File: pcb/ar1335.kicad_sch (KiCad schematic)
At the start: 46 parts

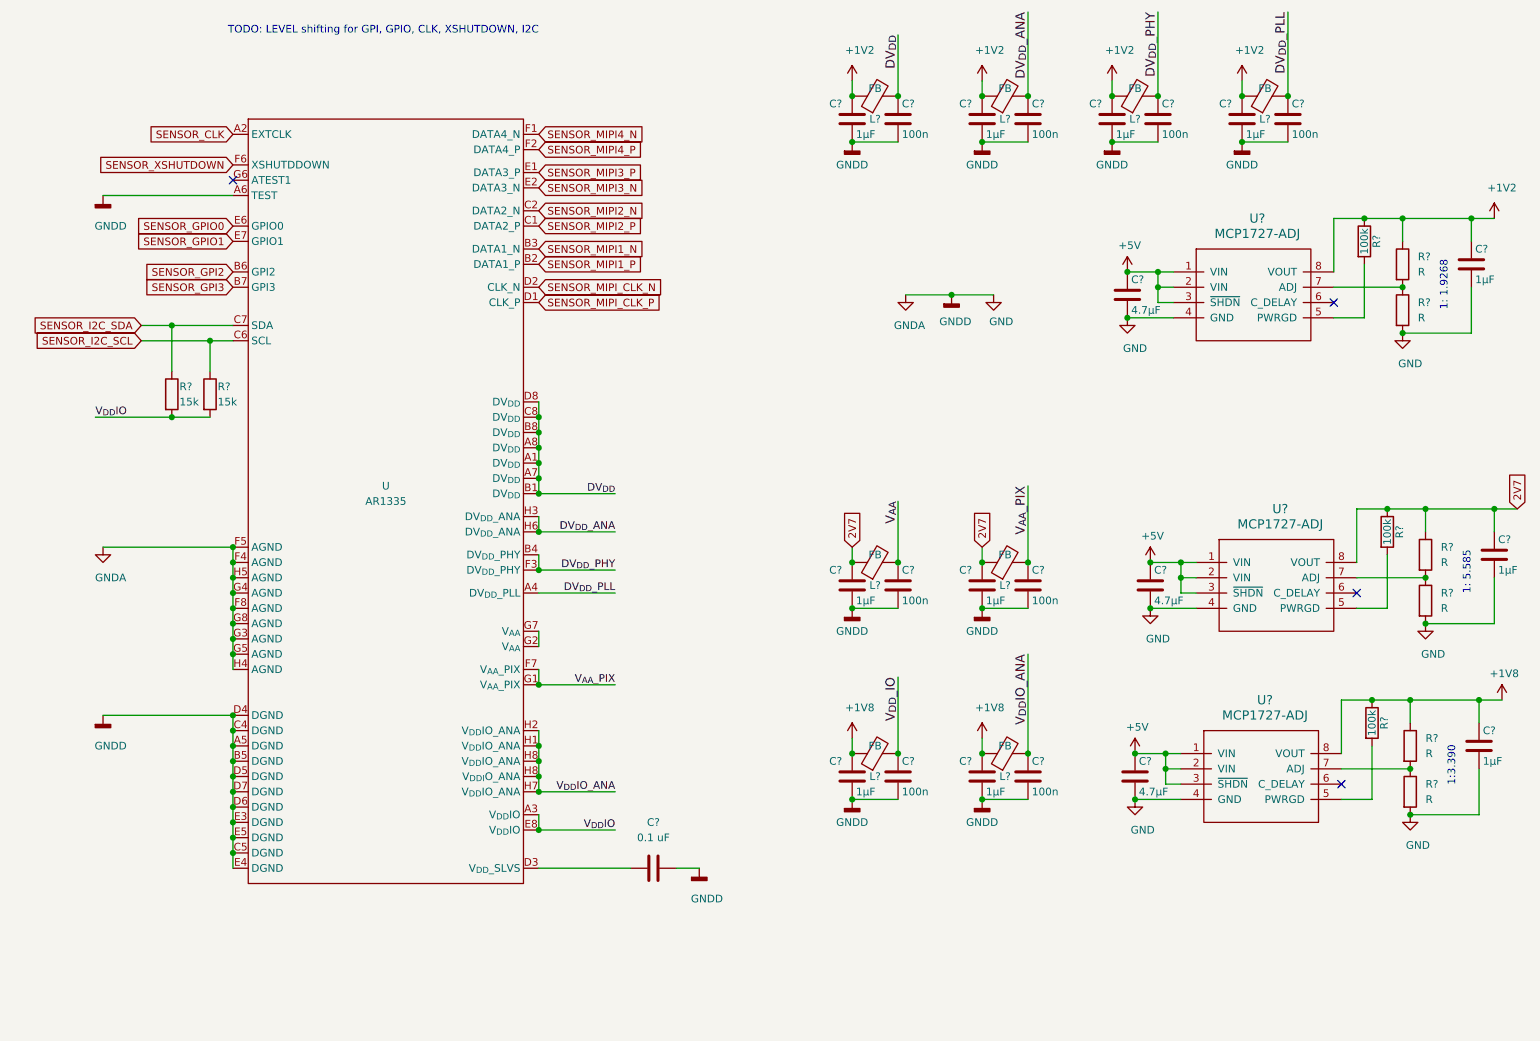
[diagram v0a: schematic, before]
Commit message: refinements; add ar1335 footprint
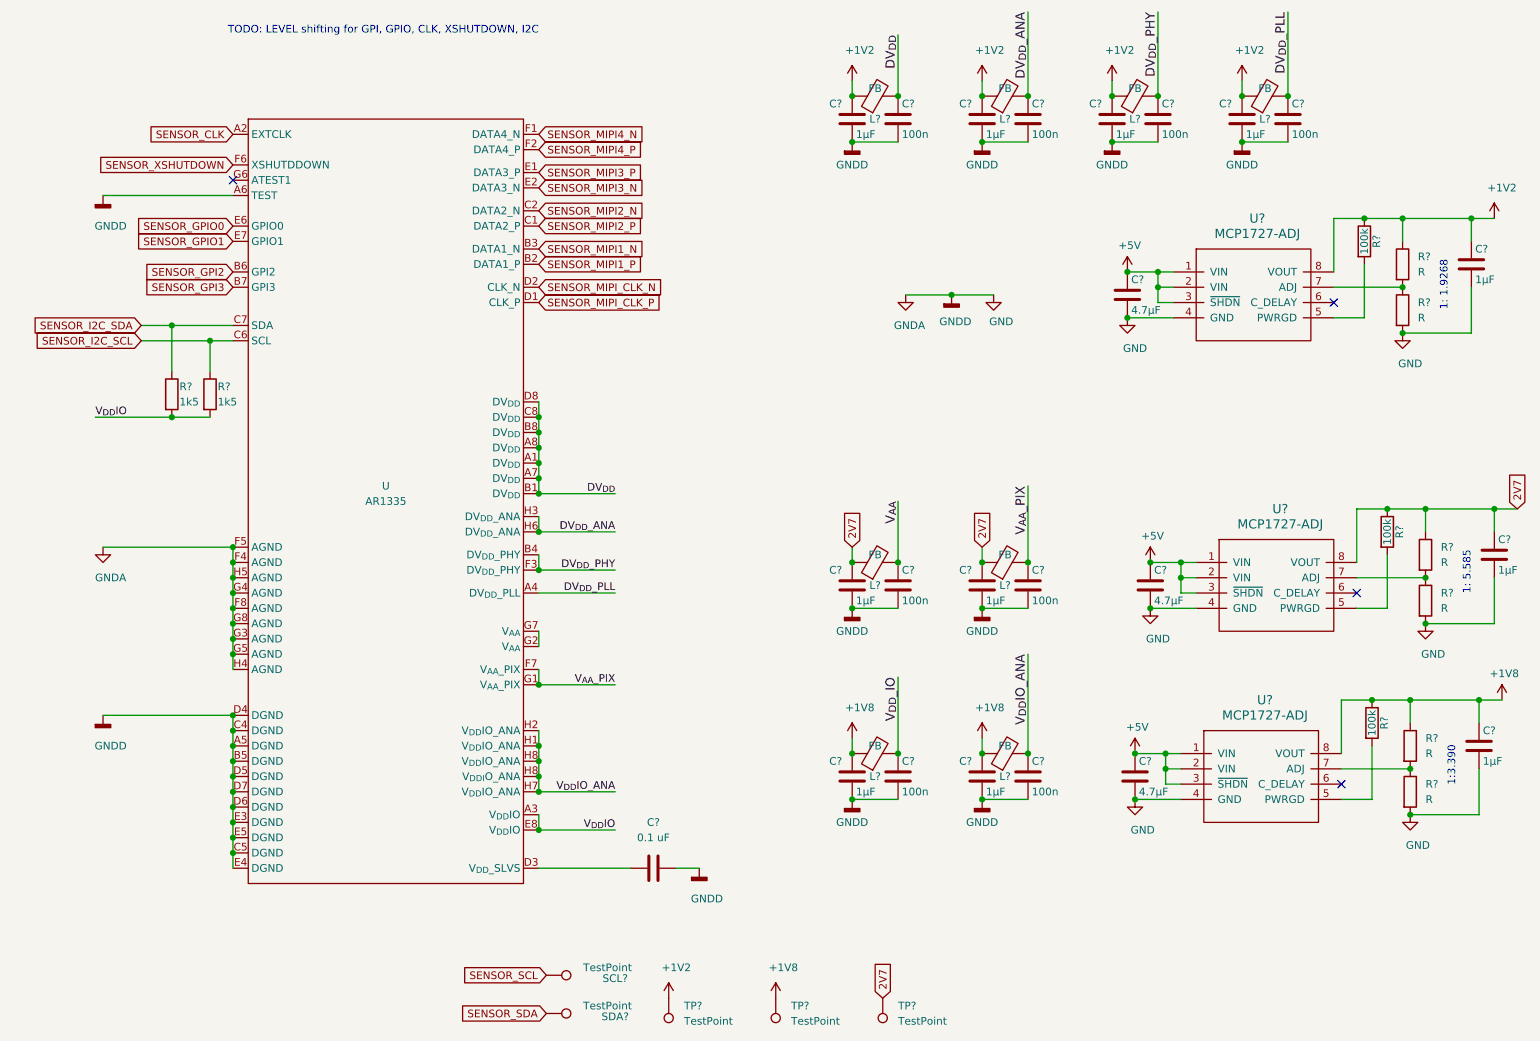
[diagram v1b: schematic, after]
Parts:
- added SCL?, SDA?: TestPoint, Connectors_TestPoints:Test_Point_Pad_2.0x2.0mm, symbol Connector:TestPoint
- added TP? (x3): TestPoint, symbol Connector:TestPoint
- R? (x2): value 15k -> 1k5
- U: footprint (none) -> ar1335:ODCSP63
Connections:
- net +1V2: now also TP?.1
- net +1V8: now also TP?.1
- net 2V7: now also TP?.1
- new net SENSOR_SCL: SCL?.1
- new net SENSOR_SDA: SDA?.1
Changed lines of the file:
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@@
     (effects (font (size 1.27 1.27)) (justify left))
+  )
+  (global_label "SENSOR_SCL" (shape input) (at 100.33 182.88 180)    (property "Intersheet References" "${INTERSHEET_REFS}" (id 0) (at 84.4186 182.8006 0)
+      (effects (font (size 1.27 1.27)) (justify right) hide)
+    )
+    (effects (font (size 1.27 1.27)) (justify right))
+  )
+  (global_label "SENSOR_SDA" (shape input) (at 100.33 189.23 180)    (property "Intersheet References" "${INTERSHEET_REFS}" (id 0) (at 84.3581 189.1506 0)
+      (effects (font (size 1.27 1.27)) (justify right) hide)
+    )
+    (effects (font (size 1.27 1.27)) (justify right))
   )
   (global_label "2V7" (shape input) (at 151.13 111.76 90)    (property "Intersheet References" "${INTERSHEET_REFS}" (id 0) (at 151.0506 104.3153 90)
@@
     (effects (font (size 1.27 1.27)) (justify left))
   )
+  (global_label "2V7" (shape input) (at 156.21 186.69 90)    (property "Intersheet References" "${INTERSHEET_REFS}" (id 0) (at 156.1306 179.2453 90)
+      (effects (font (size 1.27 1.27)) (justify left) hide)
+    )
+    (effects (font (size 1.27 1.27)) (justify left))
+  )
   (global_label "2V7" (shape input) (at 172.72 111.76 90)    (property "Intersheet References" "${INTERSHEET_REFS}" (id 0) (at 172.6406 104.3153 90)
       (effects (font (size 1.27 1.27)) (justify left) hide)
@@
     (effects (font (size 1.27 1.27)) (justify left))
   )
+  (symbol (lib_id "Connector:TestPoint") (at 100.33 182.88 270) (unit 1)
+    (in_bom yes) (on_board yes)
+    (property "Reference" "SCL?" (id 0) (at 111.76 184.15 90)
+      (effects (font (size 1.27 1.27)) (justify bottom))
+    )
+    (property "Value" "TestPoint" (id 1) (at 110.49 181.61 90))
+    (property "Footprint" "Connectors_TestPoints:Test_Point_Pad_2.0x2.0mm" (id 2) (at 100.33 182.88 0)
+      (effects (font (size 1.27 1.27)) hide)
+    )
+    (property "Datasheet" "" (id 3) (at 100.33 182.88 0)
+      (effects (font (size 1.27 1.27)) hide)
+    )
+  )
+  (symbol (lib_id "Connector:TestPoint") (at 100.33 189.23 270) (unit 1)
+    (in_bom yes) (on_board yes)
+    (property "Reference" "SDA?" (id 0) (at 111.76 190.5 90)
+      (effects (font (size 1.27 1.27)) (justify bottom))
+    )
+    (property "Value" "TestPoint" (id 1) (at 110.49 187.96 90))
+    (property "Footprint" "Connectors_TestPoints:Test_Point_Pad_2.0x2.0mm" (id 2) (at 100.33 189.23 0)
+      (effects (font (size 1.27 1.27)) hide)
+    )
+    (property "Datasheet" "" (id 3) (at 100.33 189.23 0)
+      (effects (font (size 1.27 1.27)) hide)
+    )
+  )
+  (symbol (lib_id "Connector:TestPoint") (at 120.65 186.69 180) (unit 1)
+    (in_bom yes) (on_board yes)
+    (property "Reference" "TP?" (id 0) (at 123.19 187.96 0)
+      (effects (font (size 1.27 1.27)) (justify right))
+    )
+    (property "Value" "TestPoint" (id 1) (at 123.19 190.5 0)
+      (effects (font (size 1.27 1.27)) (justify right))
+    )
+    (property "Footprint" "" (id 2) (at 115.57 186.69 0)
+      (effects (font (size 1.27 1.27)) hide)
+    )
+    (property "Datasheet" "~" (id 3) (at 115.57 186.69 0)
+      (effects (font (size 1.27 1.27)) hide)
+    )
+  )
+  (symbol (lib_id "Connector:TestPoint") (at 138.43 186.69 180) (unit 1)
+    (in_bom yes) (on_board yes)
+    (property "Reference" "TP?" (id 0) (at 140.97 187.96 0)
+      (effects (font (size 1.27 1.27)) (justify right))
+    )
+    (property "Value" "TestPoint" (id 1) (at 140.97 190.5 0)
+      (effects (font (size 1.27 1.27)) (justify right))
+    )
+    (property "Footprint" "" (id 2) (at 133.35 186.69 0)
+      (effects (font (size 1.27 1.27)) hide)
+    )
+    (property "Datasheet" "~" (id 3) (at 133.35 186.69 0)
+      (effects (font (size 1.27 1.27)) hide)
+    )
+  )
+  (symbol (lib_id "Connector:TestPoint") (at 156.21 186.69 180) (unit 1)
+    (in_bom yes) (on_board yes)
+    (property "Reference" "TP?" (id 0) (at 158.75 187.96 0)
+      (effects (font (size 1.27 1.27)) (justify right))
+    )
+    (property "Value" "TestPoint" (id 1) (at 158.75 190.5 0)
+      (effects (font (size 1.27 1.27)) (justify right))
+    )
+    (property "Footprint" "" (id 2) (at 151.13 186.69 0)
+      (effects (font (size 1.27 1.27)) hide)
+    )
+    (property "Datasheet" "~" (id 3) (at 151.13 186.69 0)
+      (effects (font (size 1.27 1.27)) hide)
+    )
+  )
+  (symbol (lib_id "power:+1V2") (at 120.65 186.69 0) (unit 1)
+    (in_bom yes) (on_board yes)
+    (property "Reference" "#PWR?" (id 0) (at 120.65 190.5 0)
+      (effects (font (size 1.27 1.27)) hide)
+    )
+    (property "Value" "+1V2" (id 1) (at 121.92 181.61 0))
+    (property "Footprint" "" (id 2) (at 120.65 186.69 0)
+      (effects (font (size 1.27 1.27)) hide)
+    )
+    (property "Datasheet" "" (id 3) (at 120.65 186.69 0)
+      (effects (font (size 1.27 1.27)) hide)
+    )
+  )
+  (symbol (lib_id "power:+1V8") (at 138.43 186.69 0) (unit 1)
+    (in_bom yes) (on_board yes)
+    (property "Reference" "#PWR?" (id 0) (at 138.43 190.5 0)
+      (effects (font (size 1.27 1.27)) hide)
+    )
+    (property "Value" "+1V8" (id 1) (at 139.7 181.61 0))
+    (property "Footprint" "" (id 2) (at 138.43 186.69 0)
+      (effects (font (size 1.27 1.27)) hide)
+    )
+    (property "Datasheet" "" (id 3) (at 138.43 186.69 0)
+      (effects (font (size 1.27 1.27)) hide)
+    )
+  )
   (symbol (lib_id "power:+1V2") (at 151.13 34.29 0) (unit 1)
     (in_bom yes) (on_board yes)
@@
       (effects (font (size 1.27 1.27)) (justify left))
     )
-    (property "Value" "15k" (id 1) (at 39.37 87.63 0)
+    (property "Value" "1k5" (id 1) (at 39.37 87.63 0)
       (effects (font (size 1.27 1.27)) (justify left))
     )
@@
       (effects (font (size 1.27 1.27)) (justify left))
     )
-    (property "Value" "15k" (id 1) (at 45.72 87.63 0)
+    (property "Value" "1k5" (id 1) (at 45.72 87.63 0)
       (effects (font (size 1.27 1.27)) (justify left))
     )
@@
     (property "Reference" "U" (id 0) (at 73.66 101.6 0))
     (property "Value" "AR1335" (id 1) (at 73.66 104.14 0))
-    (property "Footprint" "" (id 2) (at 73.66 107.95 0)
-      (effects (font (size 1.27 1.27)) hide)
-    )
+    (property "Footprint" "ar1335:ODCSP63" (id 2) (at 73.66 107.95 0)
+      (effects (font (size 1.27 1.27)) hide)
+    )

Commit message: Change Plans: two image sensors
* Redo power management
* Add level shifters
* Intention to use both image sensors on the same board
* Add Pmod & LEDs
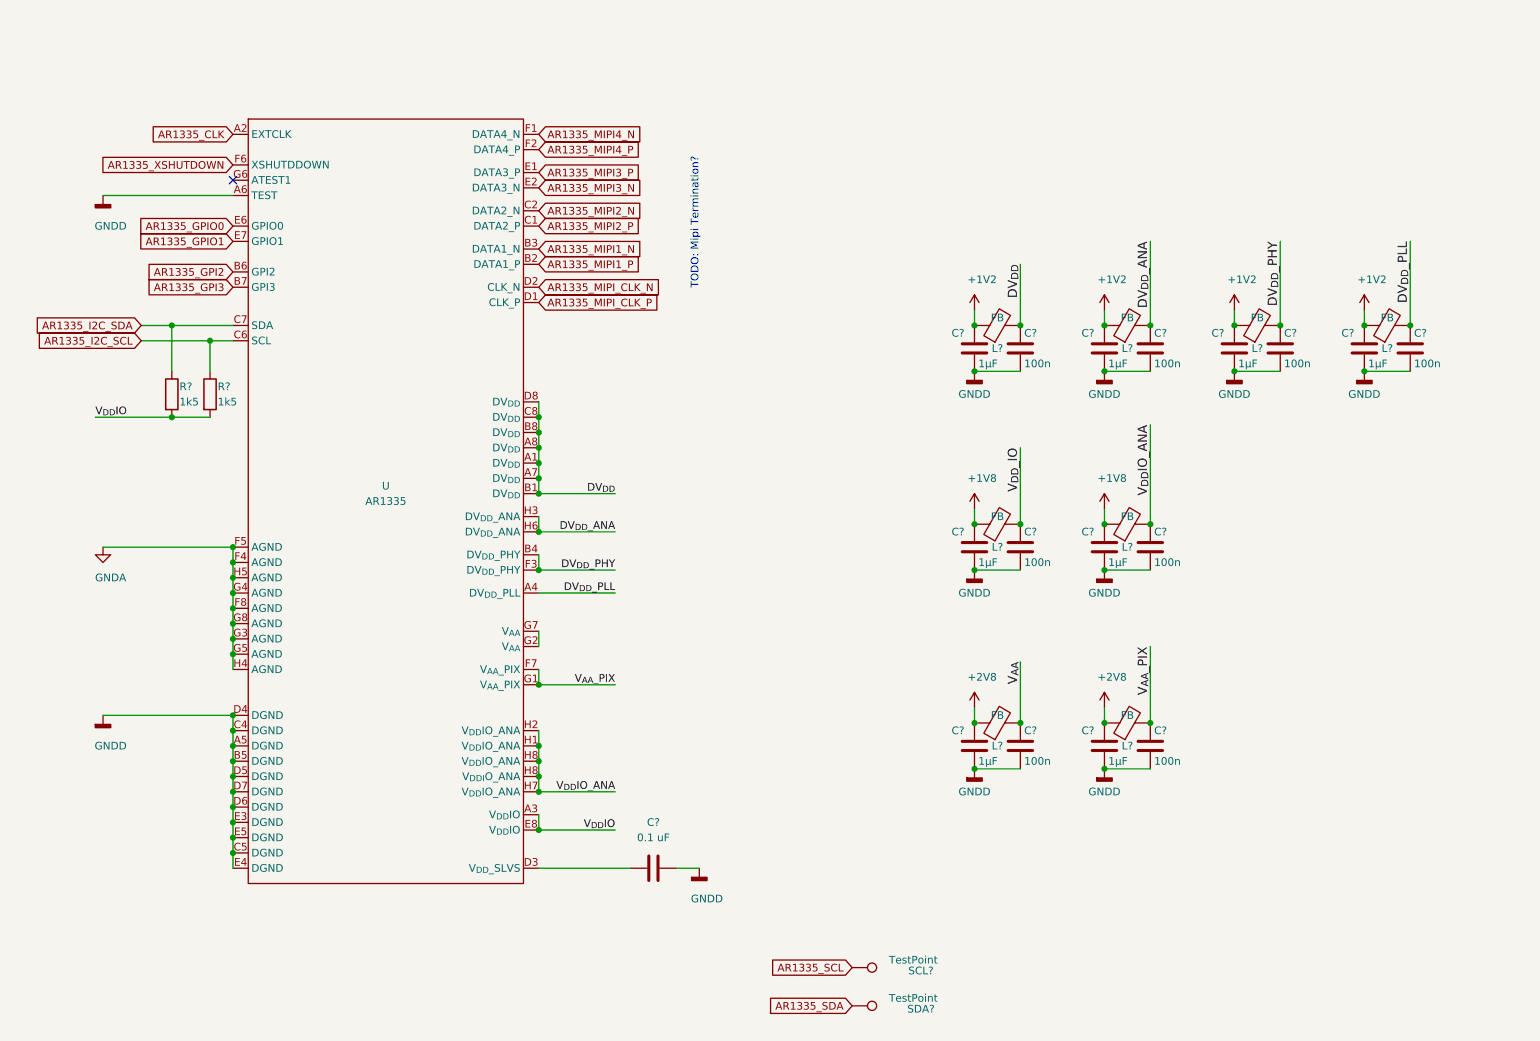
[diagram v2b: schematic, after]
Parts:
- removed C? (x3): 4.7µF, Capacitors_SMD:C_0603_HandSoldering, symbol Device:C
- removed C? (x3): 1µF, Capacitors_SMD:C_0402, symbol Device:C
- removed R? (x6): R, symbol Device:R
- removed R? (x3): 100k, Resistors_SMD:R_0603_HandSoldering, symbol Device:R
- removed TP? (x3): TestPoint, symbol Connector:TestPoint
- removed U? (x3): MCP1727-ADJ, symbol parts:MCP1727-ADJ
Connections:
- net 2V7 renamed +2V8
- net GND renamed GNDD
- net GNDD: no longer U.F4 (AGND), U.F5 (AGND), U.F8 (AGND), U.G3 (AGND), U.G4 (AGND), U.G5 (AGND), U.G8 (AGND), U.H4 (AGND), U.H5 (AGND)
- net SENSOR_CLK renamed AR1335_CLK
- net SENSOR_GPI2 renamed AR1335_GPI2
- net SENSOR_GPI3 renamed AR1335_GPI3
- net SENSOR_GPIO0 renamed AR1335_GPIO0
- net SENSOR_GPIO1 renamed AR1335_GPIO1
- net SENSOR_I2C_SCL renamed AR1335_I2C_SCL
- net SENSOR_I2C_SDA renamed AR1335_I2C_SDA
- net SENSOR_MIPI1_N renamed AR1335_MIPI1_N
- net SENSOR_MIPI1_P renamed AR1335_MIPI1_P
- net SENSOR_MIPI2_N renamed AR1335_MIPI2_N
- net SENSOR_MIPI2_P renamed AR1335_MIPI2_P
- net SENSOR_MIPI3_N renamed AR1335_MIPI3_N
- net SENSOR_MIPI3_P renamed AR1335_MIPI3_P
- net SENSOR_MIPI4_N renamed AR1335_MIPI4_N
- net SENSOR_MIPI4_P renamed AR1335_MIPI4_P
- net SENSOR_MIPI_CLK_N renamed AR1335_MIPI_CLK_N
- net SENSOR_MIPI_CLK_P renamed AR1335_MIPI_CLK_P
- net SENSOR_SCL renamed AR1335_SCL
- net SENSOR_SDA renamed AR1335_SDA
- net SENSOR_XSHUTDOWN renamed AR1335_XSHUTDOWN
- new net GNDA: U.F4 (AGND), U.F5 (AGND), U.F8 (AGND), U.G3 (AGND), U.G4 (AGND), U.G5 (AGND), U.G8 (AGND), U.H4 (AGND), U.H5 (AGND)
- no-connect marks 4 -> 1
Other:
- note added: "TODO: Mipi Termination?"
- note removed: "1: 1.9268"
- note removed: "1: 5.585"
- note removed: "1:3.390"
- note removed: "TODO: LEVEL shifting for GPI, GPIO, CLK, XSHUTDOWN, I2C"
- moved on the sheet: C?, L?, SCL?, SDA?

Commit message: add i2c addresses
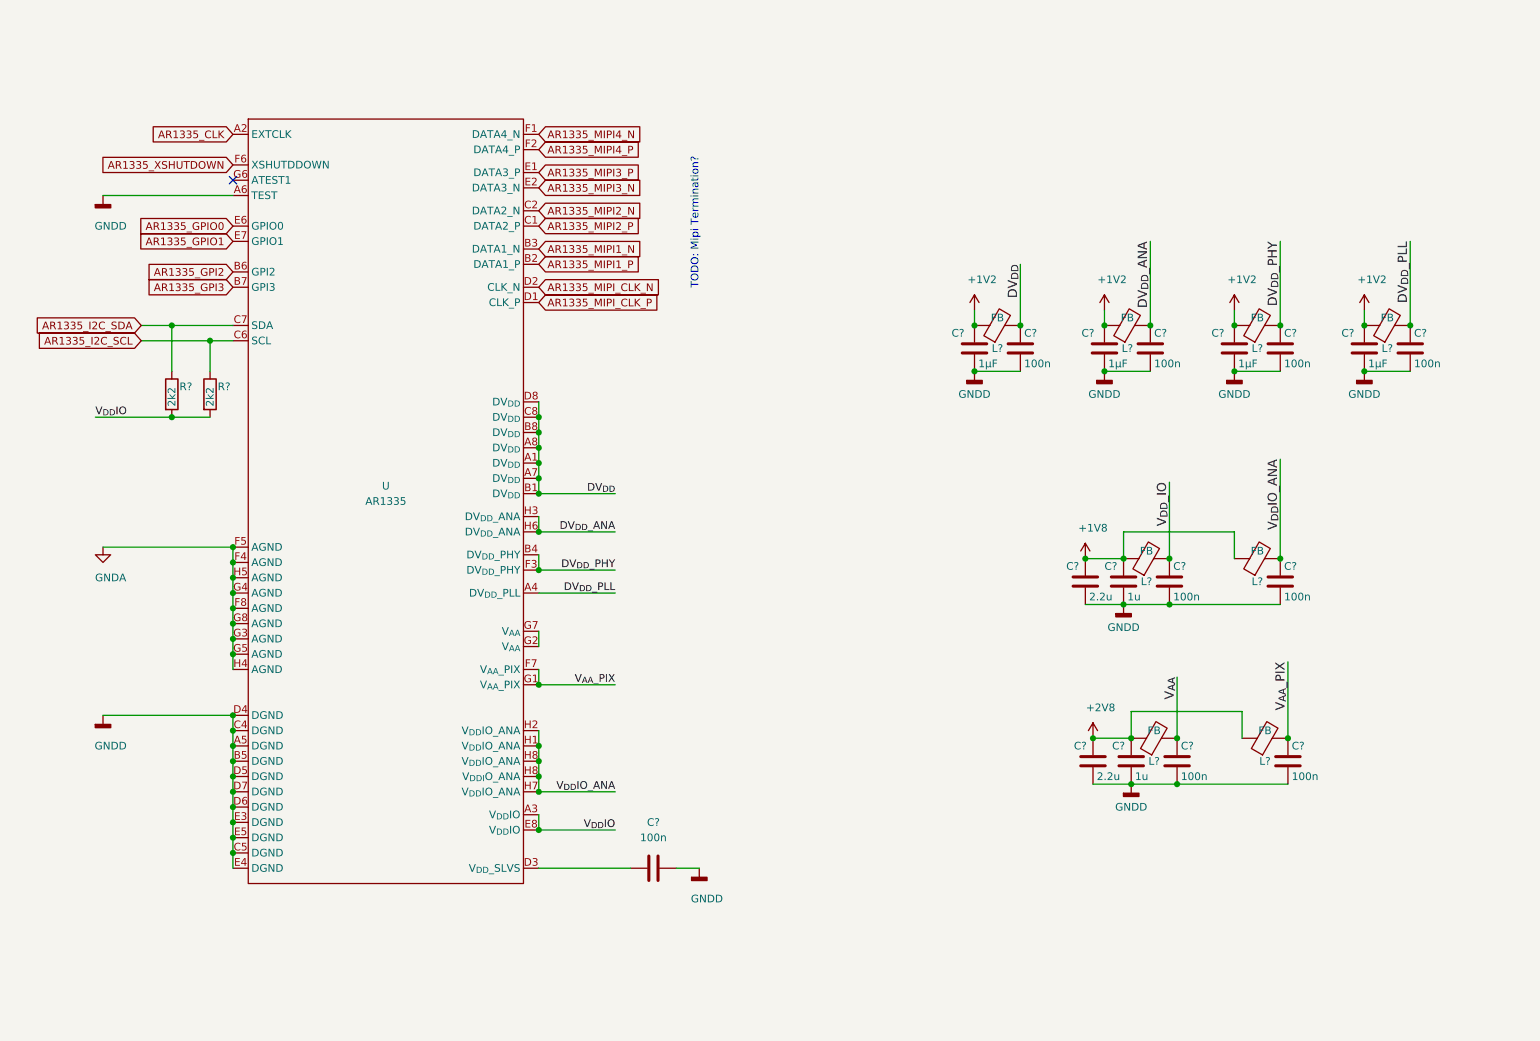
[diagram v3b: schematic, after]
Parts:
- removed C? (x3): 1µF, Capacitors_SMD:C_0402, symbol Device:C
- removed C? (x2): 100n, Capacitors_SMD:C_0402, symbol Device:C
- removed L? (x2): FB, parts:ferrite_bead_0402_handsoldering, symbol Device:FerriteBead
- removed SCL?, SDA?: TestPoint, Connectors_TestPoints:Test_Point_Pad_2.0x2.0mm, symbol Connector:TestPoint
- added C? (x2): 100n, Capacitors_SMD:C_0402, symbol Device:C
- added C? (x2): 2.2u, symbol Device:C
- added C?: 1u, Capacitors_SMD:C_0402, symbol Device:C
- added L? (x2): FB, parts:ferrite_bead_0402_handsoldering, symbol Device:FerriteBead
- C?: value 0.1 uF -> 100n
- C?: value 1µF -> 1u
- R? (x2): value 1k5 -> 2k2
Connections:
- net +1V8: now also C?.1, C?.1, L?.1, L?.1
- net +2V8: now also C?.1
- net GNDD: now also C?.2, C?.2, C?.2, C?.2, C?.2
- net V_{DD}IO_ANA: now also C?.1, L?.2
- net V_{DD}_IO: now also C?.1, L?.2
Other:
- moved on the sheet: C?, L?
